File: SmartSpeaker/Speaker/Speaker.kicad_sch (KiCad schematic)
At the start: 14 parts, among them Q1 DMG2305UX-13, U1 LM384, U2 LTC1655LCN8, U4 LM4040LP-3

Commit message: add footprints, test points
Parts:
- added TP5, TP6, TP7: TestPoint, symbol Connector:TestPoint
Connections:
- net Adafruit_1713_Microphone/output: now also TP7.1
- net Power_converter/VoltageIn: now reaches C7.1, U1.14 (VS)
- net at C6.2, R2.1, U1.6 (-): now also TP6.1
- net at C5.1, R1.1, U1.8: now also TP5.1
- net Power_converter/5VOut: now reaches Q1.3 (D)
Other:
- sheet Power_converter ports: added 5VOut, Ground, VoltageIn; removed none

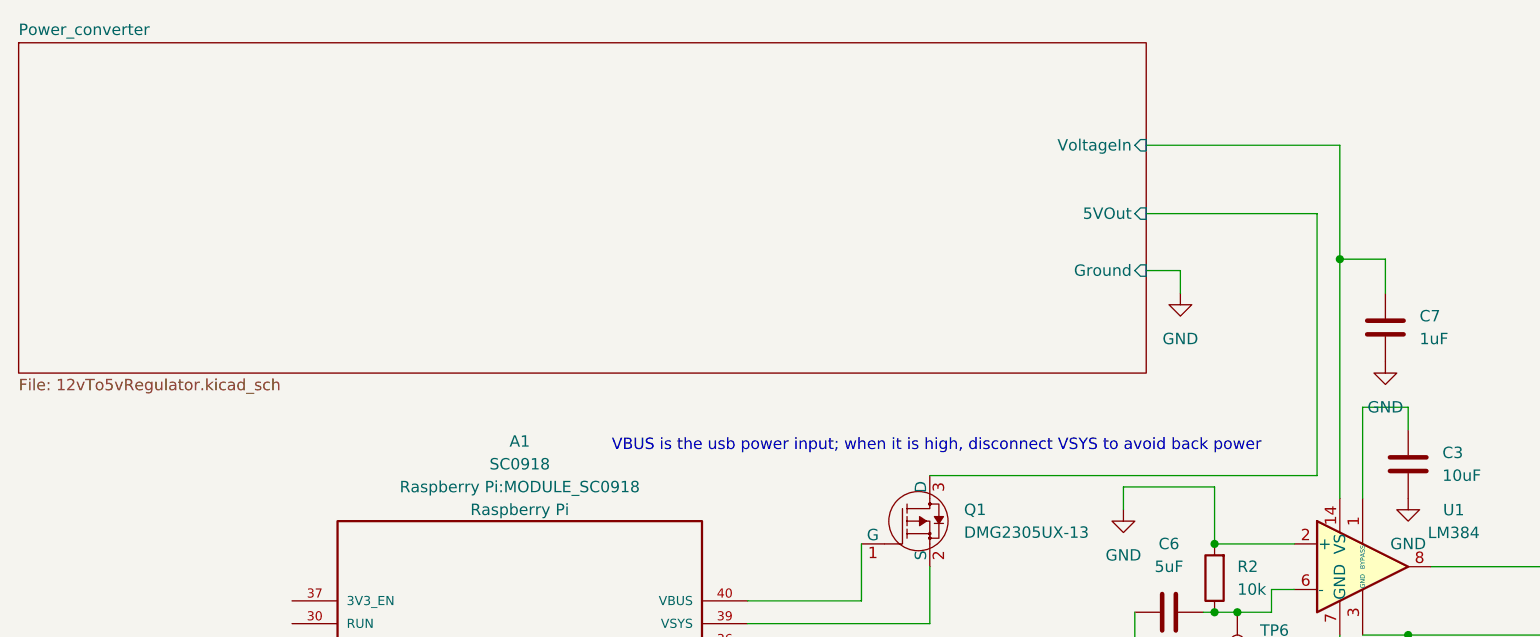
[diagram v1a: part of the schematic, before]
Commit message: add more footprints
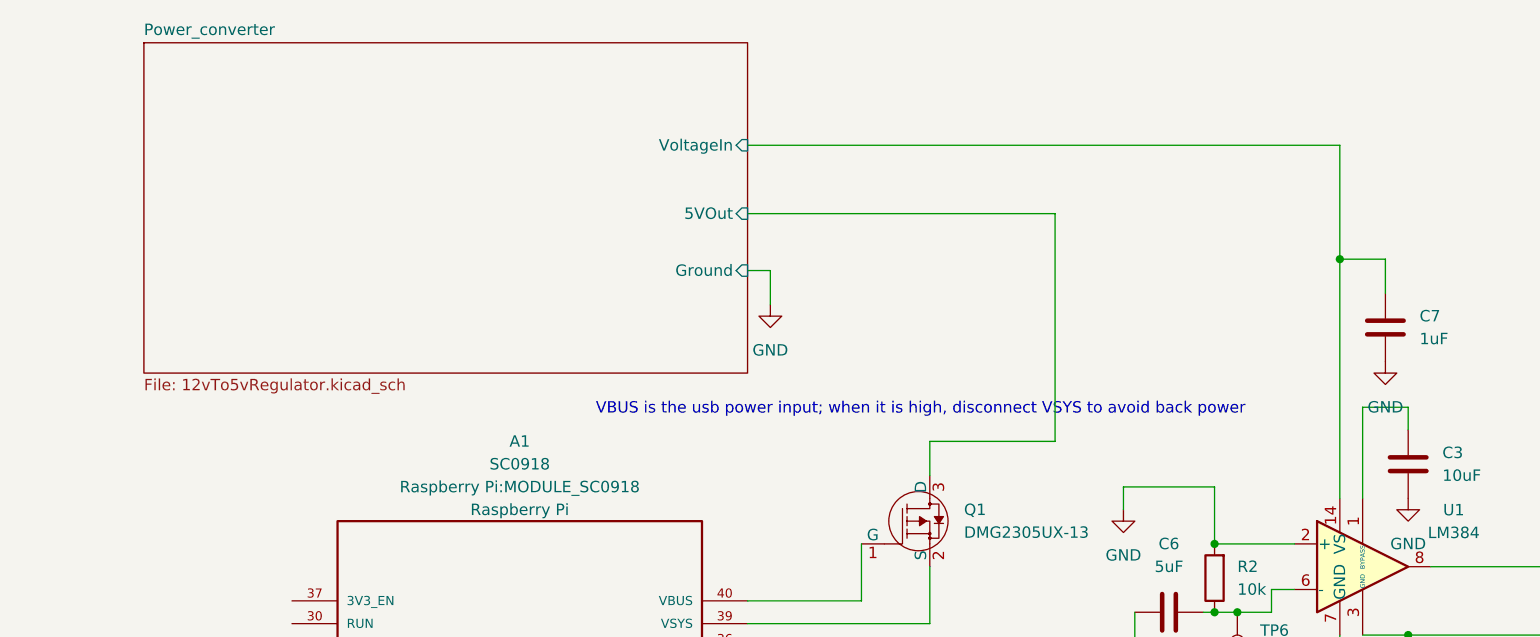
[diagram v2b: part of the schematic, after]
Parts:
- C10, C3, C4, C6, C7: footprint (none) -> Capacitor_THT:C_Disc_D7.5mm_W4.4mm_P5.00mm
- R1, R2: footprint (none) -> Resistor_THT:R_Axial_DIN0207_L6.3mm_D2.5mm_P15.24mm_Horizontal
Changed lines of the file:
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@@
+	(wire
+		(pts
+			(xy 121.92 59.69) (xy 121.92 63.5)
+		)
+		(stroke
+			(width 0)
+			(type default)
+		)
+	)
 	(wire
 		(pts
@@
 	(wire
 		(pts
-			(xy 165.1 34.29) (xy 165.1 63.5)
+			(xy 135.89 34.29) (xy 135.89 59.69)
 		)
 		(stroke
@@
 	(wire
 		(pts
-			(xy 149.86 40.64) (xy 146.05 40.64)
+			(xy 104.14 40.64) (xy 101.6 40.64)
 		)
 		(stroke
@@
 	(wire
 		(pts
-			(xy 146.05 34.29) (xy 165.1 34.29)
+			(xy 101.6 34.29) (xy 135.89 34.29)
 		)
 		(stroke
@@
 	(wire
 		(pts
-			(xy 165.1 63.5) (xy 121.92 63.5)
-		)
-		(stroke
-			(width 0)
-			(type default)
-		)
-	)
-	(wire
-		(pts
-			(xy 146.05 26.67) (xy 167.64 26.67)
+			(xy 135.89 59.69) (xy 121.92 59.69)
+		)
+		(stroke
+			(width 0)
+			(type default)
+		)
+	)
+	(wire
+		(pts
+			(xy 101.6 26.67) (xy 167.64 26.67)
 		)
 		(stroke
@@
 	(wire
 		(pts
-			(xy 149.86 43.18) (xy 149.86 40.64)
+			(xy 104.14 40.64) (xy 104.14 44.45)
 		)
 		(stroke
@@
 	(text "VBUS is the usb power input; when it is high, disconnect VSYS to avoid back power"
 		(exclude_from_sim no)
-		(at 122.682 60.198 0)
+		(at 120.904 56.134 0)
 		(effects
 			(font
@@
 			)
 		)
-		(property "Footprint" ""
+		(property "Footprint" "Capacitor_THT:C_Disc_D7.5mm_W4.4mm_P5.00mm"
 			(at 173.6852 50.8 0)
 			(effects
@@
 	(symbol
 		(lib_id "power:GND")
-		(at 149.86 43.18 0)
+		(at 104.14 44.45 0)
 		(unit 1)
 		(exclude_from_sim no)
@@
 		(fields_autoplaced yes)
 		(property "Reference" "#PWR02"
-			(at 149.86 49.53 0)
+			(at 104.14 50.8 0)
 			(effects
 				(font
@@
 		)
 		(property "Value" "GND"
-			(at 149.86 48.26 0)
+			(at 104.14 49.53 0)
 			(effects
 				(font
@@
 		)
 		(property "Footprint" ""
-			(at 149.86 43.18 0)
+			(at 104.14 44.45 0)
 			(effects
 				(font
@@
 		)
 		(property "Datasheet" ""
-			(at 149.86 43.18 0)
+			(at 104.14 44.45 0)
 			(effects
 				(font
@@
 		)
 		(property "Description" "Power symbol creates a global label with name \"GND\" , ground"
-			(at 149.86 43.18 0)
+			(at 104.14 44.45 0)
 			(effects
 				(font
@@
 			)
 		)
-		(property "Footprint" ""
+		(property "Footprint" "Capacitor_THT:C_Disc_D7.5mm_W4.4mm_P5.00mm"
 			(at 176.2252 66.04 0)
 			(effects
@@
 			)
 		)
-		(property "Footprint" ""
+		(property "Footprint" "Resistor_THT:R_Axial_DIN0207_L6.3mm_D2.5mm_P15.24mm_Horizontal"
 			(at 195.072 69.85 90)
 			(effects
@@
 			)
 		)
-		(property "Footprint" ""
+		(property "Footprint" "Capacitor_THT:C_Disc_D7.5mm_W4.4mm_P5.00mm"
 			(at 152.4 77.7748 0)
 			(effects
@@
 			)
 		)
-		(property "Footprint" ""
+		(property "Footprint" "Capacitor_THT:C_Disc_D7.5mm_W4.4mm_P5.00mm"
 			(at 197.8152 81.28 0)
 			(effects
@@
 			)
 		)
-		(property "Footprint" ""
+		(property "Footprint" "Resistor_THT:R_Axial_DIN0207_L6.3mm_D2.5mm_P15.24mm_Horizontal"
 			(at 155.448 74.93 90)
 			(effects
@@
 			)
 		)
-		(property "Footprint" ""
+		(property "Footprint" "Capacitor_THT:C_Disc_D7.5mm_W4.4mm_P5.00mm"
 			(at 120.3452 100.33 0)
 			(effects
@@
 	)
 	(sheet
-		(at 20.32 15.24)
-		(size 125.73 36.83)
+		(at 34.29 15.24)
+		(size 67.31 36.83)
 		(fields_autoplaced yes)
 		(stroke
@@
 		)
 		(property "Sheetname" "Power_converter"
-			(at 20.32 14.5284 0)
+			(at 34.29 14.5284 0)
 			(effects
 				(font
@@
 		)
 		(property "Sheetfile" "12vTo5vRegulator.kicad_sch"
-			(at 20.32 52.6546 0)
+			(at 34.29 52.6546 0)
 			(effects
 				(font
@@
 		)
 		(pin "5VOut" input
-			(at 146.05 34.29 0)
+			(at 101.6 34.29 0)
 			(effects
 				(font
@@
 		)
 		(pin "Ground" input
-			(at 146.05 40.64 0)
+			(at 101.6 40.64 0)
 			(effects
 				(font
@@
 		)
 		(pin "VoltageIn" input
-			(at 146.05 26.67 0)
-			(effects
-				(font
+			(at 101.6 26.67 0)
+			(effects
+				(font

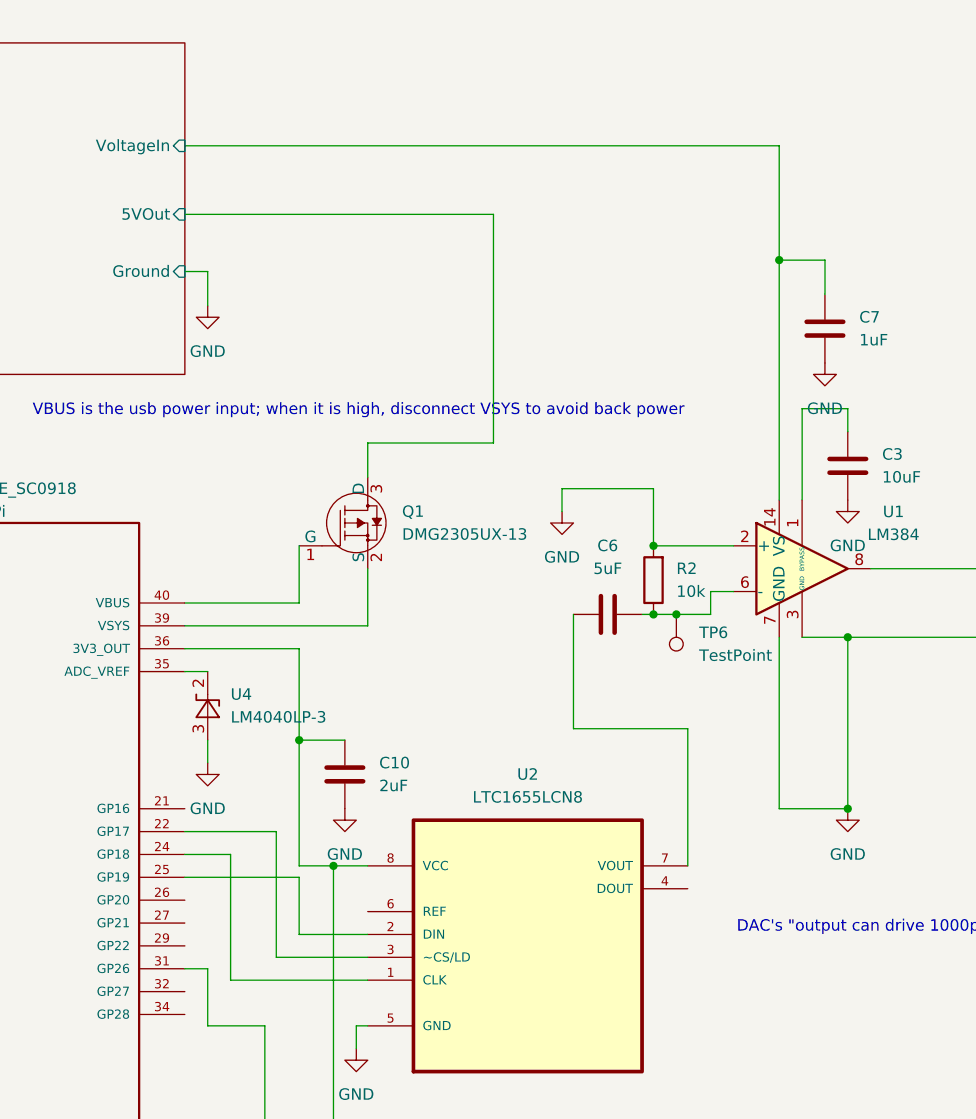
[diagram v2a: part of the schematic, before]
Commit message: add footprints for test points, jumpers
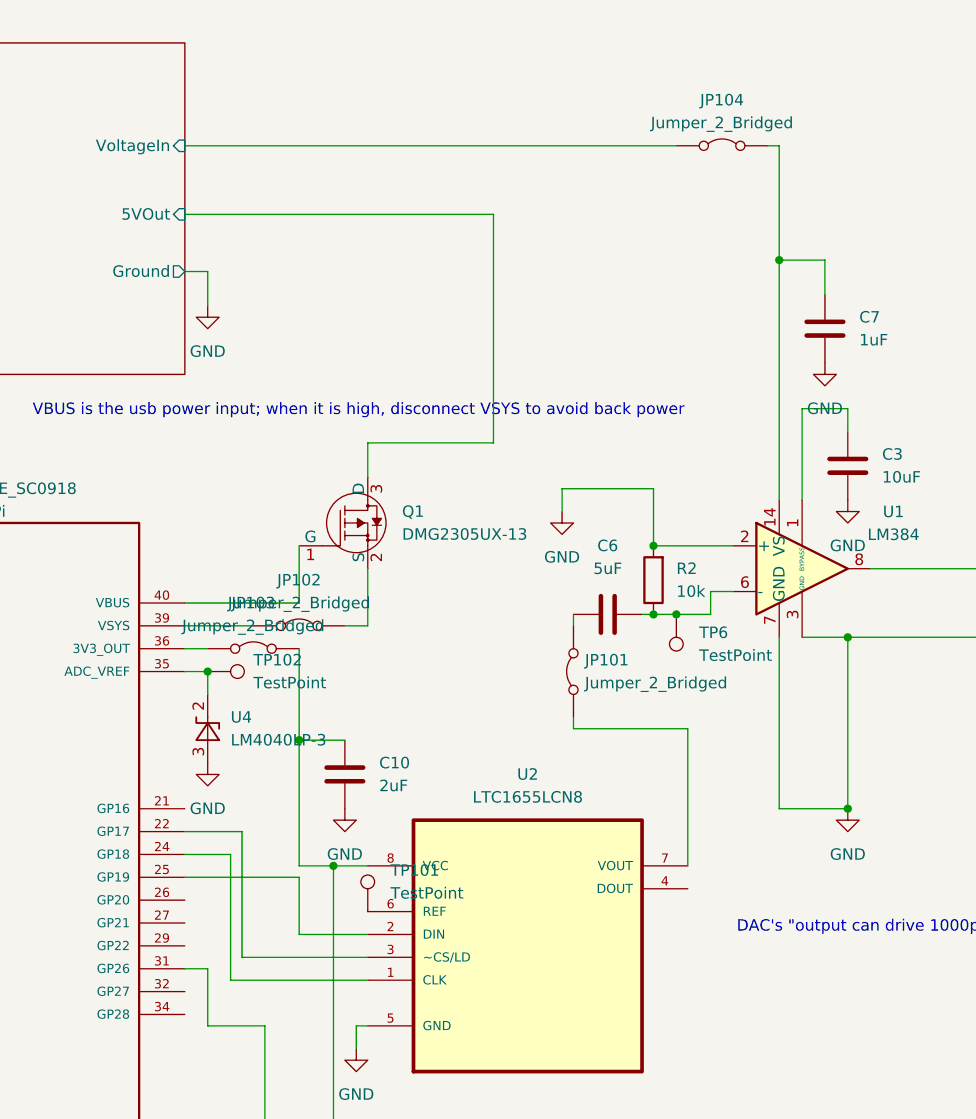
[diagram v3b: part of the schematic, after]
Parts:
- added JP101, JP102, JP103, JP104: Jumper_2_Bridged, TestPoint:TestPoint_2Pads_Pitch2.54mm_Drill0.8mm, symbol Jumper:Jumper_2_Bridged
- added TP101, TP102: TestPoint, TestPoint:TestPoint_THTPad_D2.5mm_Drill1.2mm, symbol Connector:TestPoint
- TP5, TP6, TP7: footprint (none) -> TestPoint:TestPoint_THTPad_D2.5mm_Drill1.2mm
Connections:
- net Adafruit_1713_Microphone/VCC_3.3V: now also JP103.2 (B); no longer A1.36 (3V3_OUT)
- net Power_converter/VoltageIn: now also JP104.1 (A); no longer C7.1, U1.14 (VS)
- net at U2.6 (REF): now also TP101.1
- net at U2.7 (VOUT): now also JP101.1 (A); no longer C6.1
- net at A1.35 (ADC_VREF), U4.2 (K): now also TP102.1
- net at Q1.2 (S): now also JP102.2 (B); no longer A1.39 (VSYS)
- new net: C7.1, JP104.2 (B), U1.14 (VS)
- new net: A1.36 (3V3_OUT), JP103.1 (A)
- new net: A1.39 (VSYS), JP102.1 (A)
- new net: C6.1, JP101.2 (B)
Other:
- moved on the sheet: U4

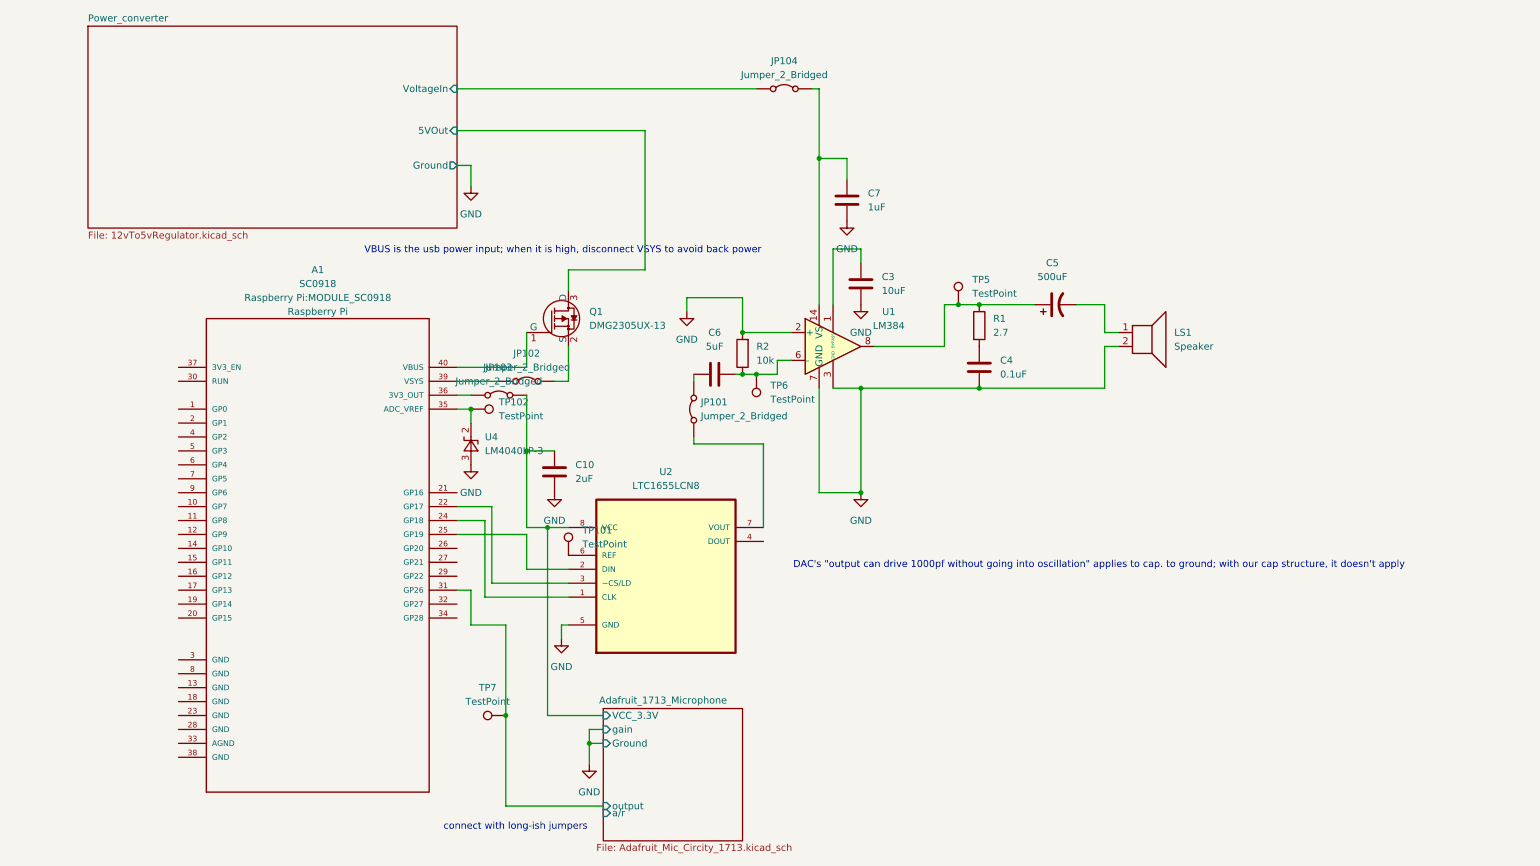
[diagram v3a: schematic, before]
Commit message: Fix some footprint problems, work towards a PCB
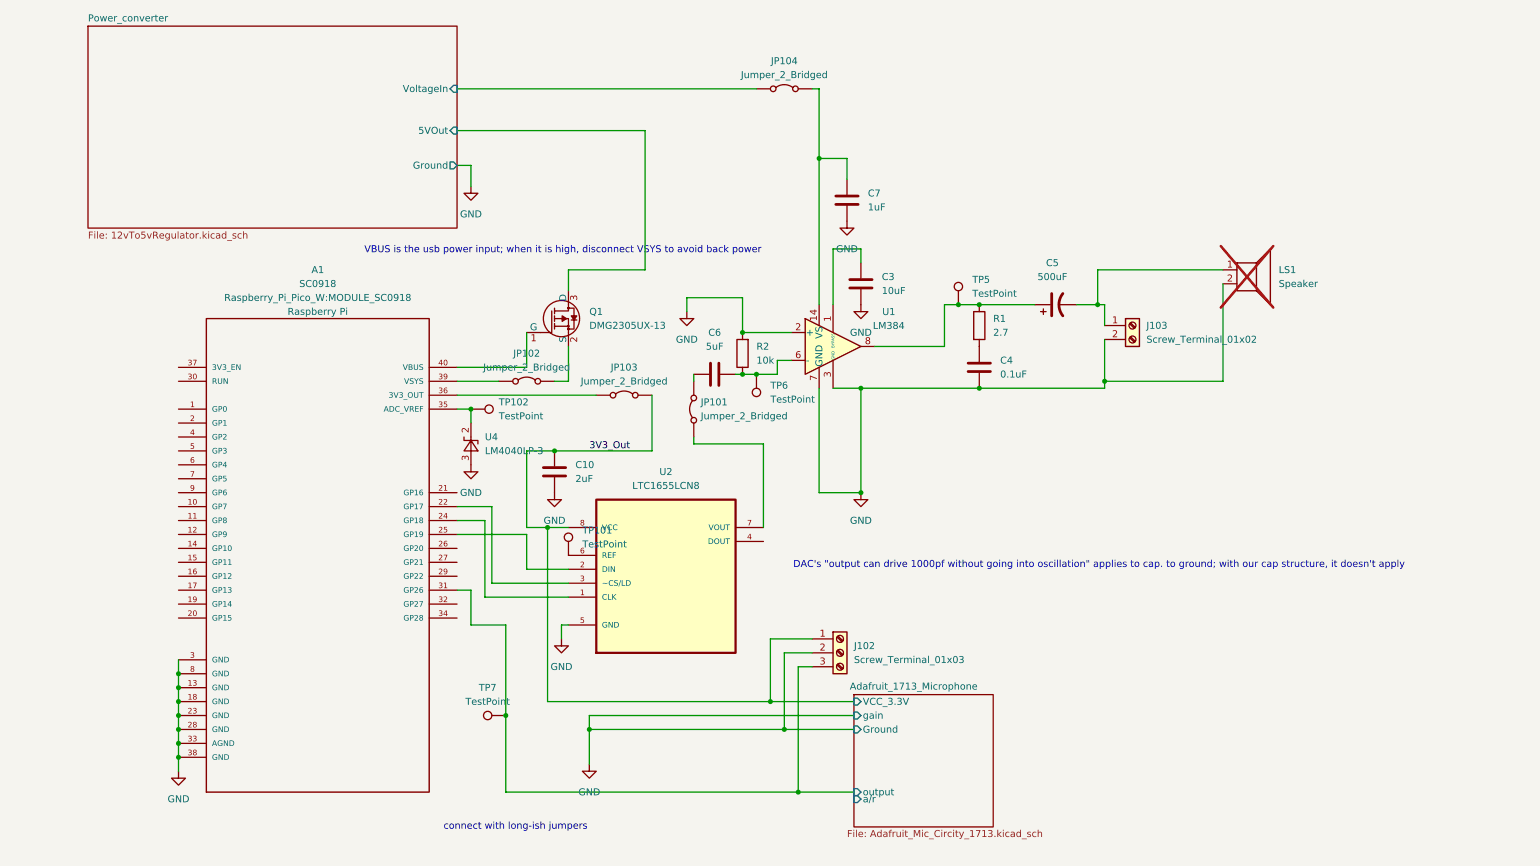
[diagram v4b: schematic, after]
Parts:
- added J102: Screw_Terminal_01x03, symbol Connector:Screw_Terminal_01x03
- added J103: Screw_Terminal_01x02, TerminalBlock_Phoenix:TerminalBlock_Phoenix_PT-1,5-2-3.5-H_1x02_P3.50mm_Horizontal, symbol Connector:Screw_Terminal_01x02
- A1: footprint Raspberry Pi:MODULE_SC0918 -> Raspberry_Pi_Pico_W:MODULE_SC0918
- C5: footprint (none) -> Capacitor_THT:CP_Radial_D12.5mm_P5.00mm
- LS1: now not fitted
- Q1: footprint digikey-footprints:SOT-23-3 -> Package_TO_SOT_SMD:SOT-23-3
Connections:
- net Adafruit_1713_Microphone/output: now also J102.3 (Pin_3)
- net GND: now also A1.13 (GND), A1.18 (GND), A1.23 (GND), A1.28 (GND), A1.3 (GND), A1.33 (AGND), A1.38 (GND), A1.8 (GND), J102.2 (Pin_2), J103.2 (Pin_2)
- net at C5.2, LS1.1: now also J103.1 (Pin_1)
- net Adafruit_1713_Microphone/VCC_3.3V renamed 3V3_Out
- net 3V3_Out: now also J102.1 (Pin_1)
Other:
- moved on the sheet: JP103

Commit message: PCB progress
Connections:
- net AudioOut: now reaches C5.1, R1.1, TP5.1, U1.8
- net SpeakerOut: now reaches C5.2, J103.1 (Pin_1), LS1.1
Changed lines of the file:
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@@
+		)
+	)
+	(label "SpeakerOut"
+		(at 222.25 59.69 0)
+		(effects
+			(font
+				(size 1.27 1.27)
+			)
+			(justify left bottom)
+		)
+	)
+	(label "AudioOut"
+		(at 181.61 73.66 0)
+		(effects
+			(font
+				(size 1.27 1.27)
+			)
+			(justify left bottom)
 		)
 	)

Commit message: PCB almost done
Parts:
- J102: footprint (none) -> TerminalBlock_Phoenix:TerminalBlock_Phoenix_PT-1,5-3-3.5-H_1x03_P3.50mm_Horizontal
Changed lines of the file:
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@@
 			)
 		)
-		(property "Footprint" ""
+		(property "Footprint" "TerminalBlock_Phoenix:TerminalBlock_Phoenix_PT-1,5-3-3.5-H_1x03_P3.50mm_Horizontal"
 			(at 171.45 129.54 0)
 			(effects
